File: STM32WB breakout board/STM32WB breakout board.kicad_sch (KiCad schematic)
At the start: 25 parts, among them J1 Conn_02x10_Counter_Clockwise, J2 Conn_02x10_Counter_Clockwise, J4 Conn_02x10_Counter_Clockwise, J5 Conn_02x10_Counter_Clockwise, U1 STM32WB15CCU6, X1 32 MHz, X2 32.768 kHz

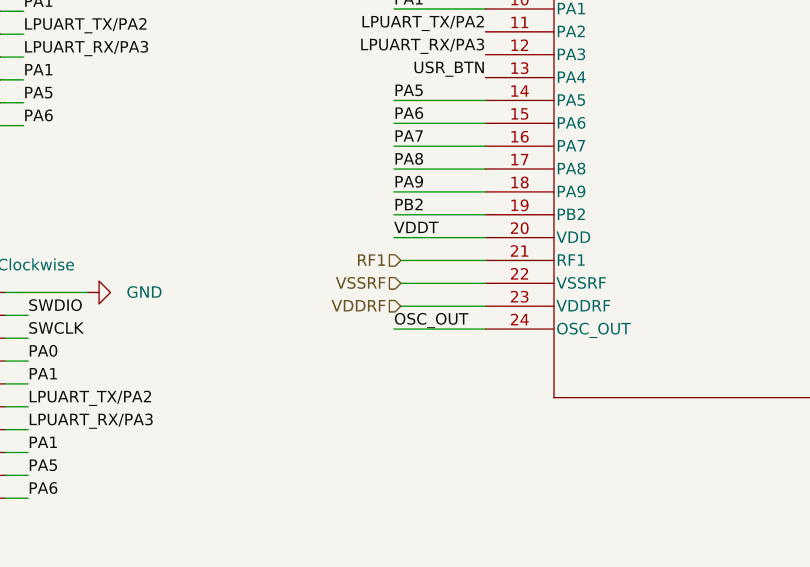
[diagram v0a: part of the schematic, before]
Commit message: Regulator section updating
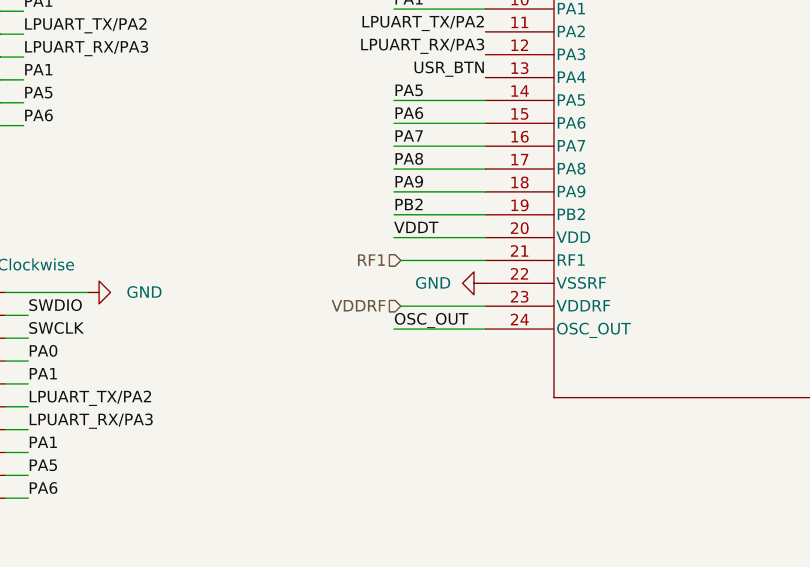
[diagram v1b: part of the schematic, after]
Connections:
- net VSSRF is gone; now on net GND: U1.22 (VSSRF)
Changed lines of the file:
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@@
-    (stroke (width 0) (type default))
-  )
-  (wire (pts (xy 101.092 81.28) (xy 110.49 81.28))
     (stroke (width 0) (type default))
   )
@@
   (hierarchical_label "VDDSMPS" (shape input) (at 176.53 66.04 0) (fields_autoplaced)
     (effects (font (size 1.27 1.27)) (justify left))
-  )
-  (hierarchical_label "VSSRF" (shape input) (at 101.092 81.28 180) (fields_autoplaced)
-    (effects (font (size 1.27 1.27)) (justify right))
   )
   (hierarchical_label "RF1" (shape input) (at 101.092 78.74 180) (fields_autoplaced)
@@
         )
       )
+    )
+  )
+  (symbol (lib_id "power:GND") (at 110.49 81.28 270) (unit 1)
+    (in_bom yes) (on_board yes) (dnp no) (fields_autoplaced)
+    (property "Reference" "#PWR026" (at 104.14 81.28 0)
+      (effects (font (size 1.27 1.27)) hide)
+    )
+    (property "Value" "GND" (at 106.68 81.28 90)
+      (effects (font (size 1.27 1.27)) (justify right))
+    )
+    (property "Footprint" "" (at 110.49 81.28 0)
+      (effects (font (size 1.27 1.27)) hide)
+    )
+    (property "Datasheet" "" (at 110.49 81.28 0)
+      (effects (font (size 1.27 1.27)) hide)
+    )
+    (pin "1")
+    (instances
+      (project "STM32WB breakout board"
+        (path "/29424def-bd0e-47af-8787-429d3d525da1"
+          (reference "#PWR026") (unit 1)
+        )
+      )

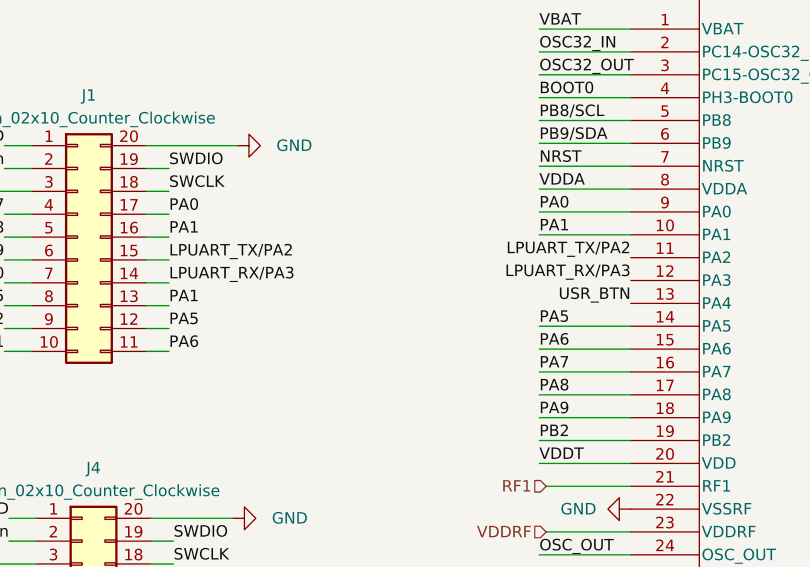
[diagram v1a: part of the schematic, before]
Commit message: Regulator section updating
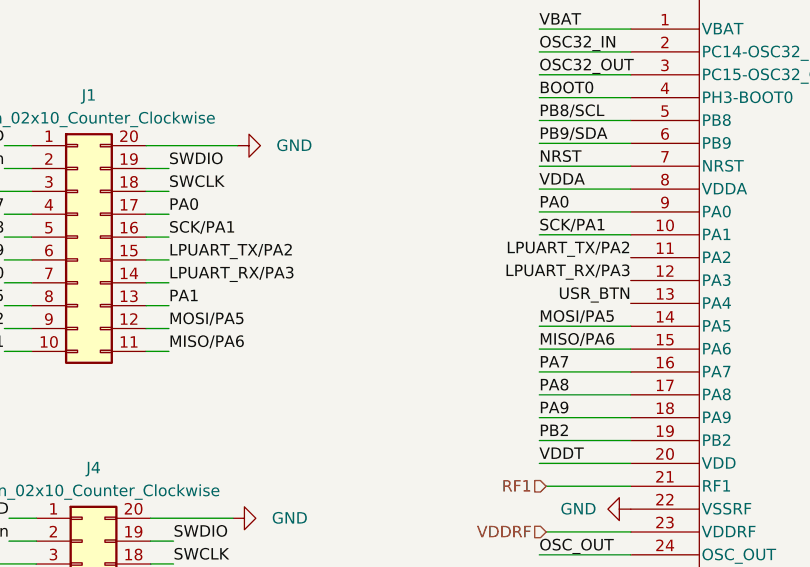
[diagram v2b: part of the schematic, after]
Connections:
- net PA1: no longer J1.16 (Pin_16), U1.10 (PA1)
- net PA5: no longer J1.12 (Pin_12), U1.14 (PA5)
- net PA6: no longer J1.11 (Pin_11), U1.15 (PA6)
- new net MISO/PA6: J1.11 (Pin_11), U1.15 (PA6)
- new net MOSI/PA5: J1.12 (Pin_12), U1.14 (PA5)
- new net SCK/PA1: J1.16 (Pin_16), U1.10 (PA1)
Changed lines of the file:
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@@
     )
   )
-  (label "PA6" (at 59.182 63.754 0) (fields_autoplaced)
-    (effects (font (size 1.27 1.27)) (justify left bottom))
-  )
   (label "NRST" (at 105.41 166.878 0) (fields_autoplaced)
+    (effects (font (size 1.27 1.27)) (justify left bottom))
+  )
+  (label "MOSI{slash}PA5" (at 59.182 61.214 0) (fields_autoplaced)
     (effects (font (size 1.27 1.27)) (justify left bottom))
   )
@@
     (effects (font (size 1.27 1.27)) (justify left bottom))
   )
-  (label "PA5" (at 59.182 61.214 0) (fields_autoplaced)
-    (effects (font (size 1.27 1.27)) (justify left bottom))
-  )
   (label "PA6" (at 59.69 105.156 0) (fields_autoplaced)
     (effects (font (size 1.27 1.27)) (justify left bottom))
@@
     (effects (font (size 1.27 1.27)) (justify left bottom))
   )
-  (label "PA1" (at 59.182 51.054 0) (fields_autoplaced)
-    (effects (font (size 1.27 1.27)) (justify left bottom))
-  )
   (label "PA0" (at 100.33 48.26 0) (fields_autoplaced)
     (effects (font (size 1.27 1.27)) (justify left bottom))
@@
     (effects (font (size 1.27 1.27)) (justify left bottom))
   )
-  (label "PA6" (at 100.33 63.5 0) (fields_autoplaced)
+  (label "MISO{slash}PA6" (at 100.33 63.5 0) (fields_autoplaced)
     (effects (font (size 1.27 1.27)) (justify left bottom))
   )
@@
     (effects (font (size 1.27 1.27)) (justify left bottom))
   )
-  (label "PA1" (at 100.33 50.8 0) (fields_autoplaced)
+  (label "SCK{slash}PA1" (at 100.33 50.8 0) (fields_autoplaced)
     (effects (font (size 1.27 1.27)) (justify left bottom))
   )
@@
     (effects (font (size 1.27 1.27)) (justify right bottom))
   )
-  (label "PA5" (at 100.33 60.96 0) (fields_autoplaced)
+  (label "MOSI{slash}PA5" (at 100.33 60.96 0) (fields_autoplaced)
+    (effects (font (size 1.27 1.27)) (justify left bottom))
+  )
+  (label "SCK{slash}PA1" (at 59.182 51.054 0) (fields_autoplaced)
     (effects (font (size 1.27 1.27)) (justify left bottom))
   )
@@
     (effects (font (size 1.27 1.27)) (justify right bottom))
   )
+  (label "MISO{slash}PA6" (at 59.182 63.754 0) (fields_autoplaced)
+    (effects (font (size 1.27 1.27)) (justify left bottom))
+  )
   (label "VDDUSB" (at 186.69 50.8 0) (fields_autoplaced)

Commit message: SMD resistors updated, some issue with inductor footprint
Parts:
- R1, R2, R3: footprint Resistor_SMD:R_1218_3246Metric_Pad1.22x4.75mm_HandSolder -> Resistor_SMD:R_1206_3216Metric
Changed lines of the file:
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@@
       (effects (font (size 1.27 1.27)))
     )
-    (property "Footprint" "Resistor_SMD:R_1218_3246Metric_Pad1.22x4.75mm_HandSolder" (at 89.916 183.134 90)
+    (property "Footprint" "Resistor_SMD:R_1206_3216Metric" (at 89.916 183.134 90)
       (effects (font (size 1.27 1.27)) hide)
     )
@@
       (effects (font (size 1.27 1.27)))
     )
-    (property "Footprint" "Resistor_SMD:R_1218_3246Metric_Pad1.22x4.75mm_HandSolder" (at 228.854 129.286 90)
+    (property "Footprint" "Resistor_SMD:R_1206_3216Metric" (at 228.854 129.286 90)
       (effects (font (size 1.27 1.27)) hide)
     )
@@
       (effects (font (size 1.27 1.27)))
     )
-    (property "Footprint" "Resistor_SMD:R_1218_3246Metric_Pad1.22x4.75mm_HandSolder" (at 210.566 113.284 90)
-      (effects (font (size 1.27 1.27)) hide)
-    )
+    (property "Footprint" "Resistor_SMD:R_1206_3216Metric" (at 210.566 113.284 90)
+      (effects (font (size 1.27 1.27)) hide)
+    )

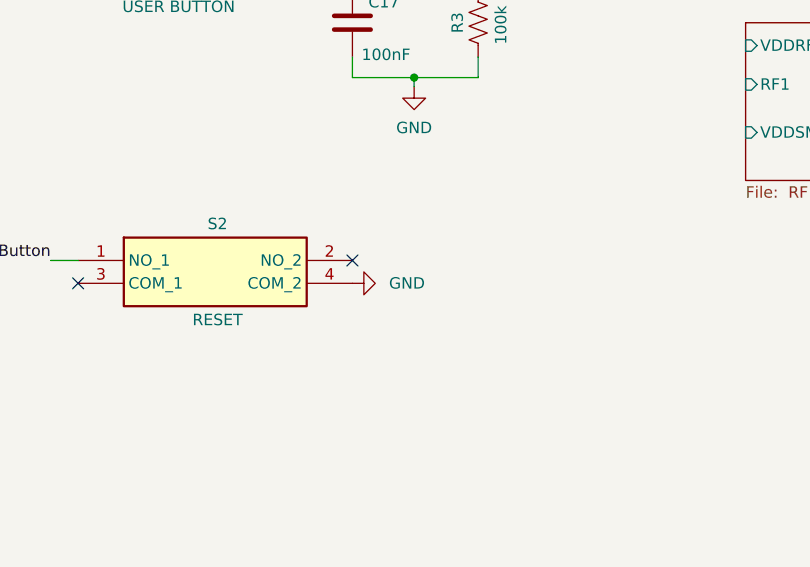
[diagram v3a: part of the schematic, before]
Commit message: L3 footprint updated
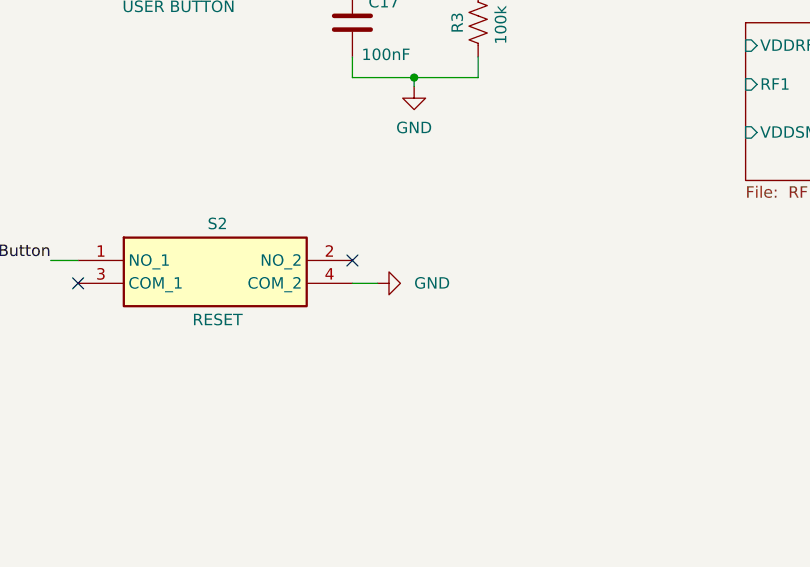
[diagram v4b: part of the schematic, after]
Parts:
- S1, S2: footprint TS026670BK160LCRD -> Button_Switch_THT:SW_PUSH_6mm
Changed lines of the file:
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@@
+    (stroke (width 0) (type default))
+  )
+  (wire (pts (xy 209.804 154.94) (xy 207.01 154.94))
     (stroke (width 0) (type default))
   )
@@
       (effects (font (size 1.27 1.27)))
     )
-    (property "Footprint" "TS026670BK160LCRD" (at 203.2 247.32 0)
+    (property "Footprint" "Button_Switch_THT:SW_PUSH_6mm" (at 203.2 247.32 0)
       (effects (font (size 1.27 1.27)) (justify left top) hide)
     )
@@
     )
   )
-  (symbol (lib_id "power:GND") (at 207.01 154.94 90) (unit 1)
+  (symbol (lib_id "power:GND") (at 209.804 154.94 90) (unit 1)
     (in_bom yes) (on_board yes) (dnp no) (fields_autoplaced)
-    (property "Reference" "#PWR021" (at 213.36 154.94 0)
-      (effects (font (size 1.27 1.27)) hide)
-    )
-    (property "Value" "GND" (at 211.074 154.94 90)
+    (property "Reference" "#PWR021" (at 216.154 154.94 0)
+      (effects (font (size 1.27 1.27)) hide)
+    )
+    (property "Value" "GND" (at 213.868 154.94 90)
       (effects (font (size 1.27 1.27)) (justify right))
     )
-    (property "Footprint" "" (at 207.01 154.94 0)
-      (effects (font (size 1.27 1.27)) hide)
-    )
-    (property "Datasheet" "" (at 207.01 154.94 0)
+    (property "Footprint" "" (at 209.804 154.94 0)
+      (effects (font (size 1.27 1.27)) hide)
+    )
+    (property "Datasheet" "" (at 209.804 154.94 0)
       (effects (font (size 1.27 1.27)) hide)
     )
@@
       (effects (font (size 1.27 1.27)))
     )
-    (property "Footprint" "TS026670BK160LCRD" (at 198.882 212.522 0)
+    (property "Footprint" "Button_Switch_THT:SW_PUSH_6mm" (at 198.882 212.522 0)
       (effects (font (size 1.27 1.27)) (justify left top) hide)
     )

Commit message: MCU Symbol updated
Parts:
- removed U1: STM32WB15CCU6, QFPN_15CCU6_STM, symbol STM32WB15CCU6:STM32WB15CCU6
- added U1: STM32WB15CCU6, Package_DFN_QFN:QFN-48-1EP_7x7mm_P0.5mm_EP5.6x5.6mm, symbol MCU_ST_STM32WB:STM32WB15CCUx
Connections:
- net 3V3: now also U1.1 (VBAT), U1.20 (VDD), U1.35 (VDD), U1.40 (VDD), U1.48 (VDD), U1.8 (VDDA)
- net BOOT0: now also U1.4 (PH3)
- net GND: now also U1.22 (VSSRF), U1.32 (VSSSMPS), U1.49 (VSS)
- net LPUART_RX/PA3: now also U1.12 (PA3)
- net LPUART_TX/PA2: now also U1.11 (PA2)
- net MISO/PA6: now also U1.15 (PA6)
- net MOSI/PA5: now also U1.14 (PA5)
- net NRST: now also U1.7 (NRST(PB11))
- net OSC32_IN: now also U1.2 (PC14)
- net OSC32_OUT: now also U1.3 (PC15)
- net OSC_IN: now also U1.25 (OSC_IN)
- net OSC_OUT: now also U1.24 (OSC_OUT)
- net PA0: now also U1.9 (PA0)
- net PA10: now also U1.36 (PA10)
- net PA11: now also U1.37 (PA11)
- net PA12: now also U1.38 (PA12)
- net PA15: now also U1.42 (PA15)
- net PA7: now also U1.16 (PA7)
- net PA8: now also U1.17 (PA8)
- net PA9: now also U1.18 (PA9)
- net PB1: now also U1.29 (PB1)
- net PB2: now also U1.19 (PB2)
- net PB3: now also U1.43 (PB3)
- net PB4: now also U1.44 (PB4)
- net PB5: now also U1.45 (PB5)
- net PB6: now also U1.46 (PB6)
- net PB7: now also U1.47 (PB7)
- net PE4: now also U1.30 (PE4)
- net RF1: now also U1.21 (RF1)
- net SCK/PA1: now also U1.10 (PA1)
- net SWCLK: now also U1.41 (PA14)
- net SWDIO: now also U1.39 (PA13)
- net USR_BTN: now also U1.13 (PA4)
- net VDDRF: now also U1.23 (VDDRF)
- net VDDSMPS: now also U1.34 (VDDSMPS)
- net VFBSMPS: now also U1.31 (VFBSMPS)
- net VLXSMPS: now also U1.33 (VLXSMPS)
- net PB8/SCL renamed SCL/PB8
- net SCL/PB8: now also U1.5 (PB8)
- net PB9/SDA renamed SDA/PB9
- net SDA/PB9: now also U1.6 (PB9)
- no-connect marks 7 -> 5
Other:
- moved on the sheet: J1, J2, J4

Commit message: schematic updated
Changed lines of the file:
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@@
+    (stroke (width 0) (type default))
+  )
+  (wire (pts (xy 244.094 128.778) (xy 246.38 128.778))
     (stroke (width 0) (type default))
   )
@@
     (stroke (width 0) (type default))
   )
+  (wire (pts (xy 272.288 132.588) (xy 274.574 132.588))
+    (stroke (width 0) (type default))
+  )
   (wire (pts (xy 82.042 166.878) (xy 82.042 171.958))
     (stroke (width 0) (type default))
@@
     (stroke (width 0) (type default))
   )
+  (wire (pts (xy 244.094 133.096) (xy 246.38 133.096))
+    (stroke (width 0) (type default))
+  )
   (wire (pts (xy 89.662 174.752) (xy 89.662 171.958))
     (stroke (width 0) (type default))
@@
     (stroke (width 0) (type default))
   )
+  (wire (pts (xy 244.348 137.414) (xy 246.38 137.414))
+    (stroke (width 0) (type default))
+  )
   (wire (pts (xy 224.536 33.528) (xy 227.076 33.528))
     (stroke (width 0) (type default))
@@
   )
   (wire (pts (xy 32.004 144.018) (xy 45.212 144.018))
+    (stroke (width 0) (type default))
+  )
+  (wire (pts (xy 272.288 128.778) (xy 274.828 128.778))
     (stroke (width 0) (type default))
   )
@@
     (effects (font (size 1.27 1.27)) (justify right bottom))
   )
+  (label "VFBSMPS" (at 122.936 50.546 180) (fields_autoplaced)
+    (effects (font (size 1.27 1.27)) (justify right bottom))
+  )
   (label "PB5" (at 224.536 36.068 180) (fields_autoplaced)
     (effects (font (size 1.27 1.27)) (justify right bottom))
@@
     (effects (font (size 1.27 1.27)) (justify right bottom))
   )
+  (label "RF1" (at 244.094 133.096 180) (fields_autoplaced)
+    (effects (font (size 1.27 1.27)) (justify right bottom))
+  )
   (label "VBAT" (at 138.176 27.686 90) (fields_autoplaced)
     (effects (font (size 1.27 1.27)) (justify left bottom))
   )
+  (label "VDDSMPS" (at 155.956 27.686 90) (fields_autoplaced)
+    (effects (font (size 1.27 1.27)) (justify left bottom))
+  )
   (label "PB3" (at 224.282 67.564 180) (fields_autoplaced)
     (effects (font (size 1.27 1.27)) (justify right bottom))
@@
   )
   (label "PB1" (at 168.656 78.486 0) (fields_autoplaced)
+    (effects (font (size 1.27 1.27)) (justify left bottom))
+  )
+  (label "VFBSMPS" (at 274.828 128.778 0) (fields_autoplaced)
     (effects (font (size 1.27 1.27)) (justify left bottom))
   )
@@
     (effects (font (size 1.27 1.27)) (justify left bottom))
   )
+  (label "RF1" (at 122.936 55.626 180) (fields_autoplaced)
+    (effects (font (size 1.27 1.27)) (justify right bottom))
+  )
   (label "PA0" (at 168.656 32.766 0) (fields_autoplaced)
     (effects (font (size 1.27 1.27)) (justify left bottom))
@@
     (effects (font (size 1.27 1.27)) (justify right bottom))
   )
+  (label "VDDRF" (at 244.094 128.778 180) (fields_autoplaced)
+    (effects (font (size 1.27 1.27)) (justify right bottom))
+  )
   (label "OSC_IN" (at 60.198 185.674 0) (fields_autoplaced)
     (effects (font (size 1.27 1.27)) (justify left bottom))
@@
     (effects (font (size 1.27 1.27)) (justify right bottom))
   )
+  (label "VDDRF" (at 153.416 27.686 90) (fields_autoplaced)
+    (effects (font (size 1.27 1.27)) (justify left bottom))
+  )
   (label "SDA{slash}PB9" (at 168.656 98.806 0) (fields_autoplaced)
     (effects (font (size 1.27 1.27)) (justify left bottom))
@@
     (effects (font (size 1.27 1.27)) (justify left bottom))
   )
+  (label "VLXSMPS" (at 122.936 37.846 180) (fields_autoplaced)
+    (effects (font (size 1.27 1.27)) (justify right bottom))
+  )
   (label "VDD" (at 143.256 27.686 90) (fields_autoplaced)
     (effects (font (size 1.27 1.27)) (justify left bottom))
@@
     (effects (font (size 1.27 1.27)) (justify right bottom))
   )
+  (label "VDDSMPS" (at 244.348 137.414 180) (fields_autoplaced)
+    (effects (font (size 1.27 1.27)) (justify right bottom))
+  )
   (label "VDDA" (at 150.876 27.686 90) (fields_autoplaced)
+    (effects (font (size 1.27 1.27)) (justify left bottom))
+  )
+  (label "VLXSMPS" (at 274.574 132.588 0) (fields_autoplaced)
     (effects (font (size 1.27 1.27)) (justify left bottom))
   )
@@
     )
   )
-  (hierarchical_label "VFBSMPS" (shape input) (at 122.936 50.546 180) (fields_autoplaced)
-    (effects (font (size 1.27 1.27)) (justify right))
-  )
-  (hierarchical_label "VLXSMPS" (shape input) (at 122.936 37.846 180) (fields_autoplaced)
-    (effects (font (size 1.27 1.27)) (justify right))
-  )
-  (hierarchical_label "VDDRF" (shape input) (at 153.416 27.686 90) (fields_autoplaced)
-    (effects (font (size 1.27 1.27)) (justify left))
-  )
-  (hierarchical_label "VDDSMPS" (shape input) (at 155.956 27.686 90) (fields_autoplaced)
-    (effects (font (size 1.27 1.27)) (justify left))
-  )
-  (hierarchical_label "RF1" (shape input) (at 122.936 55.626 180) (fields_autoplaced)
-    (effects (font (size 1.27 1.27)) (justify right))
-  )
   (symbol (lib_id "power:GND") (at 18.796 187.706 0) (unit 1)
     (in_bom yes) (on_board yes) (dnp no)
@@
   (symbol (lib_id "MCU_ST_STM32WB:STM32WB15CCUx") (at 145.796 68.326 0) (unit 1)
     (in_bom yes) (on_board yes) (dnp no)
-    (property "Reference" "U1" (at 160.274 106.934 0)
-      (effects (font (size 1.27 1.27)) (justify left))
-    )
-    (property "Value" "STM32WB15CCU6" (at 154.686 109.474 0)
+    (property "Reference" "U1" (at 120.396 90.678 0)
+      (effects (font (size 1.27 1.27)) (justify left))
+    )
+    (property "Value" "STM32WB15CCU6" (at 118.872 97.79 90)
       (effects (font (size 1.27 1.27)) (justify left))
     )
@@
     )
   )
-  (sheet (at 250.698 125.984) (size 25.908 17.526)
+  (sheet (at 246.38 126.238) (size 25.908 17.526)
     (stroke (width 0.1524) (type solid))
     (fill (color 0 0 0 0.0000))
-    (property "Sheetname" "RF & Power" (at 257.81 125.476 0)
+    (property "Sheetname" "RF & Power" (at 253.492 125.73 0)
       (effects (font (size 1.27 1.27)) (justify left bottom))
     )
-    (property "Sheetfile" " RF Section_sch.kicad_sch" (at 250.698 144.0946 0)
+    (property "Sheetfile" " RF Section_sch.kicad_sch" (at 246.38 144.3486 0)
       (effects (font (size 1.27 1.27)) (justify left top))
     )
-    (pin "VDDRF" input (at 250.698 128.524 180)
-      (effects (font (size 1.27 1.27)) (justify left))
-    )
-    (pin "RF1" input (at 250.698 132.842 180)
-      (effects (font (size 1.27 1.27)) (justify left))
-    )
-    (pin "VDDSMPS" input (at 250.698 138.176 180)
-      (effects (font (size 1.27 1.27)) (justify left))
-    )
-    (pin "VFBSMPS" input (at 276.606 128.524 0)
+    (pin "VDDRF" input (at 246.38 128.778 180)
+      (effects (font (size 1.27 1.27)) (justify left))
+    )
+    (pin "RF1" input (at 246.38 133.096 180)
+      (effects (font (size 1.27 1.27)) (justify left))
+    )
+    (pin "VDDSMPS" input (at 246.38 137.414 180)
+      (effects (font (size 1.27 1.27)) (justify left))
+    )
+    (pin "VFBSMPS" input (at 272.288 128.778 0)
       (effects (font (size 1.27 1.27)) (justify right))
     )
-    (pin "VLXSMPS" input (at 276.606 132.334 0)
+    (pin "VLXSMPS" input (at 272.288 132.588 0)
       (effects (font (size 1.27 1.27)) (justify right))
     )
